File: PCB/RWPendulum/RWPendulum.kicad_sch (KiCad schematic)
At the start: 17 parts, among them IC1 L7805CV, J1 Screw_Terminal_01x02, J2 Conn_01x06_Pin, J3 Conn_01x04_Pin, J4 Screw_Terminal_01x02, SW1 SW_SPST, SW2 SW_Push, U2 ESP32-DEVKIT-V1

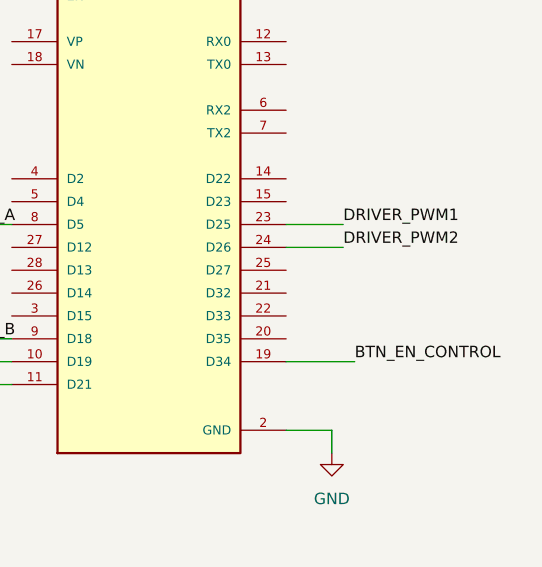
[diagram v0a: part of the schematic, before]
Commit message: PCB: Rev. 1 - Gabriel Tumang - 22/01/2026
Mudando pino do botão EN_CONTROL para 27 no lugar do 34 para utilizar função de pullup interno da ESP32,
por consequência, os pinos de PWM p/ o driver foram modvidos para facilitar o roteamento.
Também foram alterados tamanhos dos furos e pads de alguns componentes para tentar minimizar problemas de fabricação.
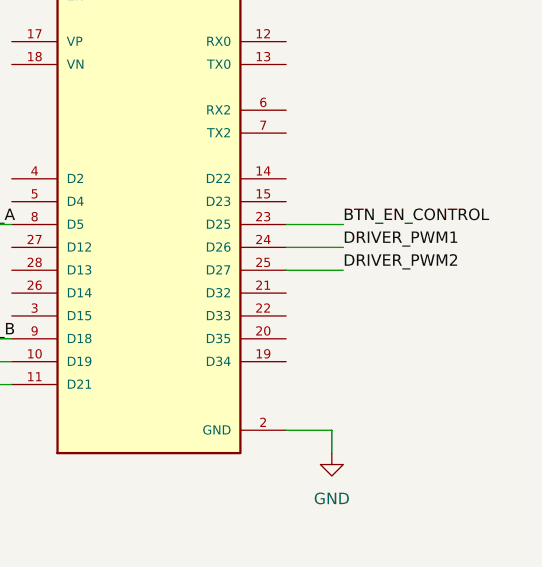
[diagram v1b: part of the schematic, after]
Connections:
- net BTN_EN_CONTROL: now also U2.23 (D25); no longer U2.19 (D34)
- net DRIVER_PWM1: now also U2.24 (D26); no longer U2.23 (D25)
- net DRIVER_PWM2: now also U2.25 (D27); no longer U2.24 (D26)
